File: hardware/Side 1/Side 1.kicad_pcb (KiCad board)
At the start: 2 copper layers, 126 x 214.2 mm, 4 parts

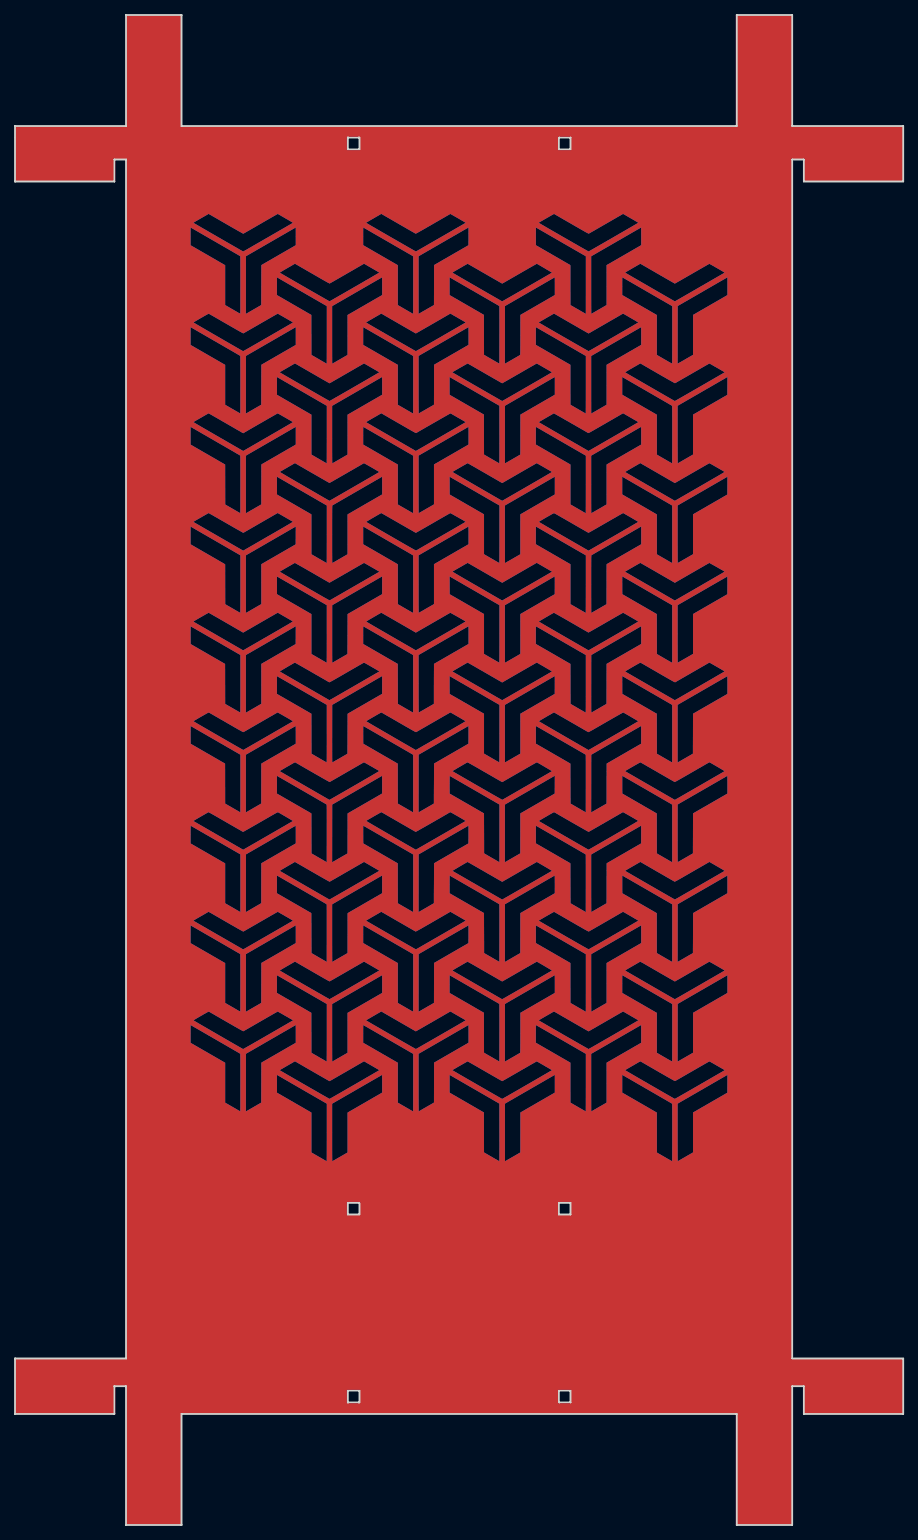
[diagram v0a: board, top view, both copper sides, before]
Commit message: Added reflective copper on inside Added version with cutout dinoskin Generated gerbers
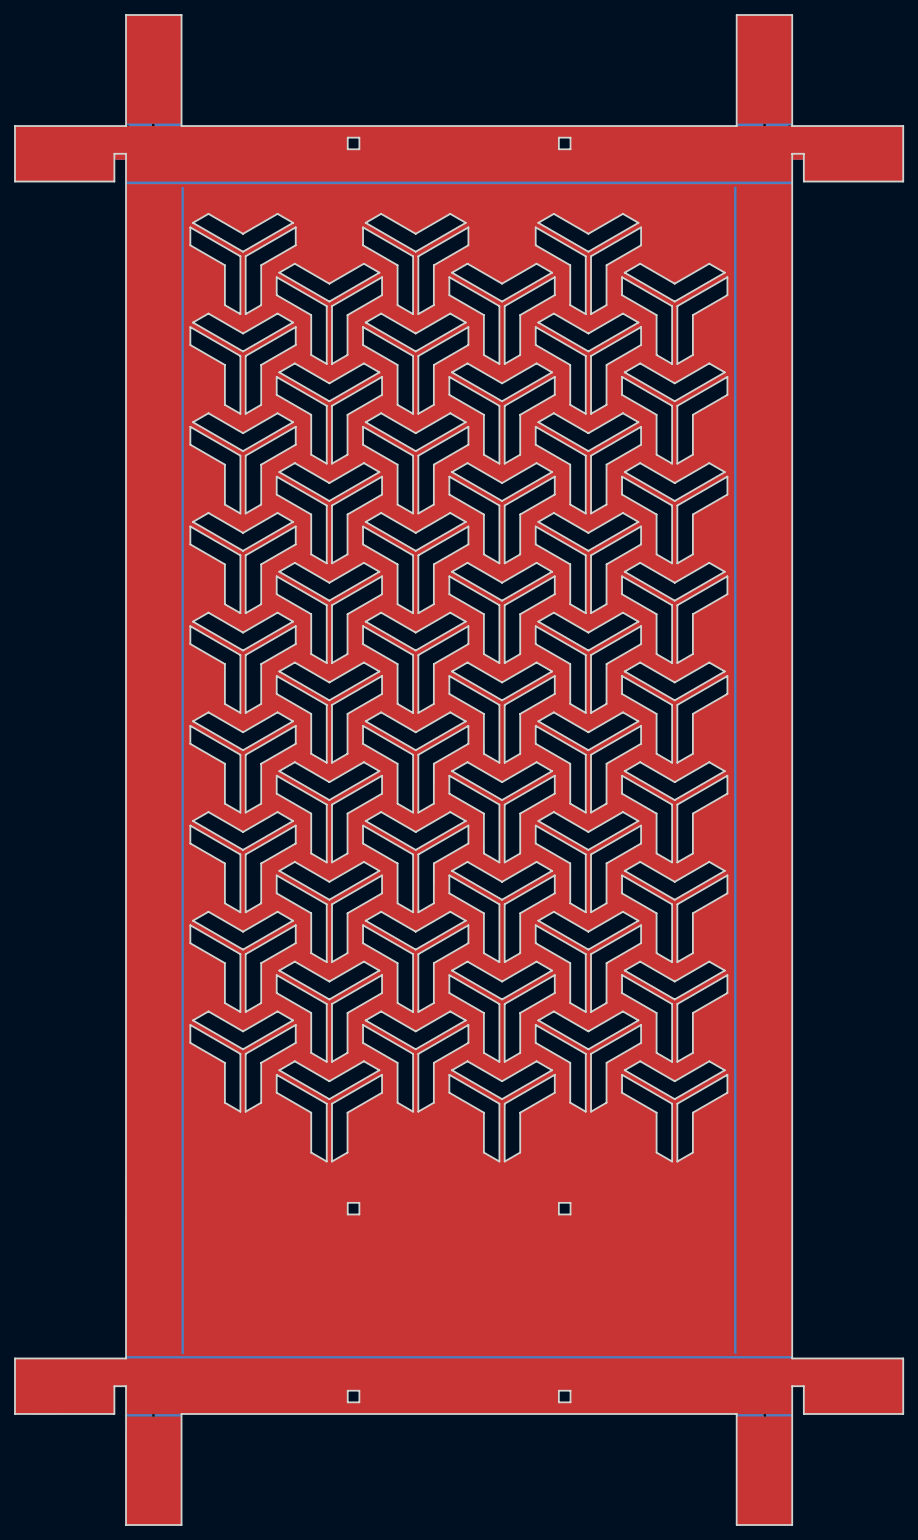
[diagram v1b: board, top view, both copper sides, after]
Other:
- outline, holes or cut-outs redrawn

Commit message: God knows but a lot has changed
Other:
- outline, holes or cut-outs redrawn
- board text added: "JLCJLCJLC"
